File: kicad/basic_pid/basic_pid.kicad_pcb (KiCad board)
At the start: 4 copper layers, 152.4 x 101.6 mm, 125 parts, among them J1 Input A, J2 Input B / Setpoint, J3 Monitor, J4 Output, J5 Screw_Terminal_01x04, J6 Screw_Terminal_01x03, SW1 SW_DPDT_x2, SW10 SW_DPDT_x2, SW2 SW_DPDT_x2, SW3 SW_DPDT_x2, SW4 SW_SP4T, SW5 SW_DPDT_x2, SW6 SW_SP4T, SW7 SW_SP4T, SW8 SW_SP4T, SW9 SW_SP4T, U1 LM4040DBZ-5, U10 OPA189, U11 OPA189, U12 OPA189, U13 BUF634A, U14 LM2940CS-12/NOPB, U15 LM2990SX-12, U16 LM317_TO-252, U2 LM4040DBZ-5, U3 INA849, U4 INA849, U5 OPA189, U6 OPA189, U7 OPA189, U8 BUF634A, U9 OPA189

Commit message: Fixed wrong part and added shunt resistor values
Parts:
- removed LOGO3: JQI-LOGOSILK, lib:JQI_LOGO_NEGATIVE-SILKSCREEN
- C1: value 100n -> 100nF
- C11: value 100p -> 10p
- C12: value 1n -> 100p
- C13: value 10n -> 1n
- C6: value 1nF -> 10nF
- C7: value 10nF -> 100nF
- C8: value 100nF -> 1uF
- C9: value 1uF -> 10uF
- R1, R2: value R_US -> 10k
- R14: value 220 -> 4.7k

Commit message: Fixed monitor instability
Added a 3.3 kOhm resistor on each output buffer's bandwith control pin
to increase the bandwidth from 30 MHz to 90 MHz.
This should prevent oscillations and instabilities we noticed while
testing the PID
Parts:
- added R35: 3.3k, Resistor_SMD:R_0805_2012Metric, F.Cu at (130.7, 44.8)
- added R36: 3.3k, Resistor_SMD:R_0805_2012Metric, F.Cu at (170.7, 40.4)
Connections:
- U13 pad 1: unconnected-(U13-BW-Pad1) -> Net-(U13-BW)
- U8 pad 1: unconnected-(U8-BW-Pad1) -> Net-(U8-BW)
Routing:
- net GND: track 40.0 -> 51.3 mm, vias 40 -> 38
- net -12V: track 51.7 -> 59.4 mm
- net Net-(U8-BW): track 0.00 -> 4.66 mm
- net Net-(U13-BW): track 0.00 -> 4.32 mm
- net Net-(U13-IN): track 15.6 -> 16.4 mm

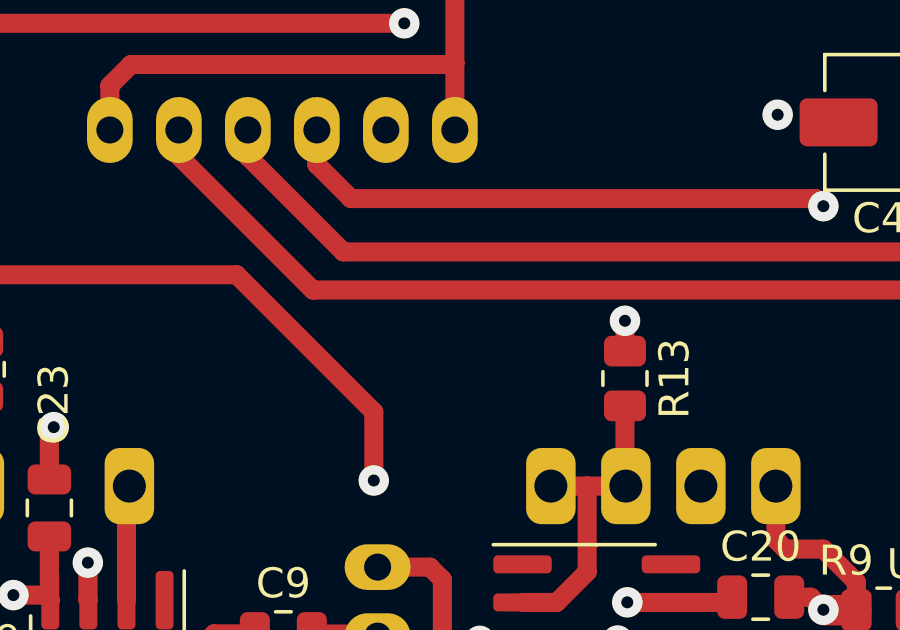
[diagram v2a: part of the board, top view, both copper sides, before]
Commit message: Not sure if it works: Just a possibile fix for a noisy monitor when sampling error signal
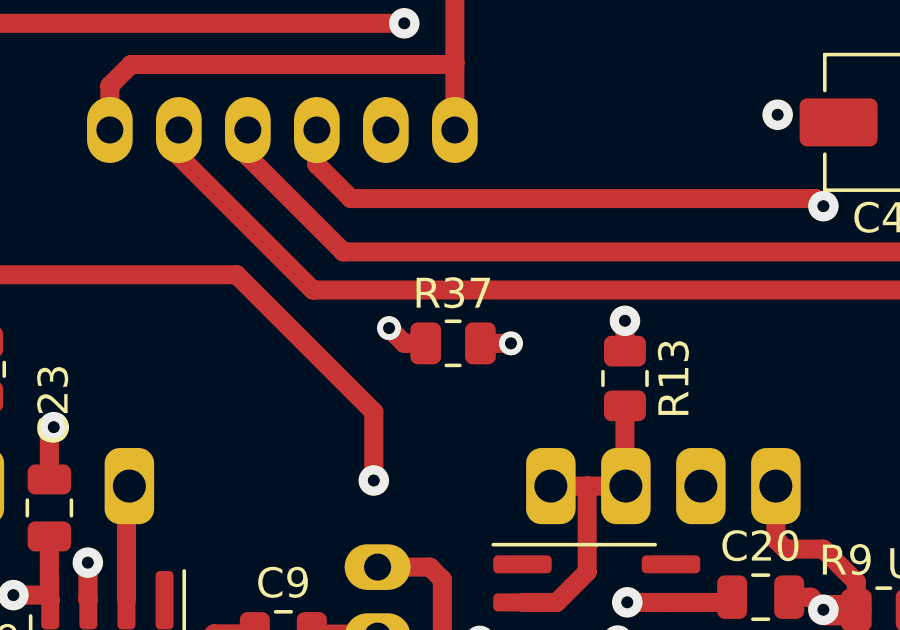
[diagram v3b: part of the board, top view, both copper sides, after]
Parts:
- added R37: 3.3k, Resistor_SMD:R_0805_2012Metric, F.Cu at (158.1, 63.0)
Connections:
- SW4 pad 4: Error_signal -> Net-(R37-Pad1)
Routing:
- net Net-(R37-Pad1): track 0.00 -> 7.93 mm, vias 0 -> 1
- net Error_signal: track 142.9 -> 135.2 mm, vias 3 -> 4
